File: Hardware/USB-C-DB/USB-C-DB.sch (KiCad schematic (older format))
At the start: 2 parts

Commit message: Updating schematic to v0.2 > Added USB to UART bridge and initial biasing > Added biasing circuitry for MCU > Moved display section to hierarchy > Simplified and consolidated power supply section > Added bypass caps for power supplies, USB interface IC and MCU
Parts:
- removed U?: PIC18F25K50-xSO, Package_SO:SOIC-28W_7.5x17.9mm_P1.27mm, symbol MCU_Microchip_PIC18:PIC18F25K50-xSO
- added C? (x6): 0.1u, Capacitor_SMD:C_0805_2012Metric_Pad1.18x1.45mm_HandSolder, symbol Device:C
- added C? (x3): 10u, Capacitor_SMD:C_0805_2012Metric_Pad1.18x1.45mm_HandSolder, symbol Device:C
- added C? (x2): 47p, Capacitor_SMD:C_0402_1005Metric_Pad0.74x0.62mm_HandSolder, symbol Device:C
- added C? (x4): 4.7u, Capacitor_SMD:C_0805_2012Metric_Pad1.18x1.45mm_HandSolder, symbol Device:C
- added J2: BatTP+, TestPoint:TestPoint_Pad_4.0x4.0mm, symbol Connector_Generic:Conn_01x01
- added J3: JST Battery con, Connector_JST:JST_PH_B2B-PH-K_1x02_P2.00mm_Vertical, symbol Connector_Generic:Conn_01x02
- added J4: BatTP-, TestPoint:TestPoint_Pad_4.0x4.0mm, symbol Connector_Generic:Conn_01x01
- added R? (x3): 5.1k, Resistor_SMD:R_0805_2012Metric_Pad1.20x1.40mm_HandSolder, symbol Device:R
- added R? (x7): 10k, Resistor_SMD:R_0603_1608Metric_Pad0.98x0.95mm_HandSolder, symbol Device:R
- added R?: 0.001, Resistor_SMD:R_2512_6332Metric_Pad1.40x3.35mm_HandSolder, symbol Device:R_Shunt
- added U1: FT260S-U, Package_SO:TSSOP-28_4.4x9.7mm_P0.65mm, symbol FT260S-U:FT260S-U
- added U3: ESP-WROOM-02, RF_Module:ESP-WROOM-02, symbol RF_Module:ESP-WROOM-02
- added U?: LD1117S33TR_SOT223, Package_TO_SOT_SMD:SOT-223-3_TabPin2, symbol Regulator_Linear:LD1117S33TR_SOT223
- J1: renamed from J?; symbol Connector:USB_C_Receptacle -> USB-C-DB-rescue:USB_C_Receptacle-Connector
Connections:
- net labels added: +3.3V, +BATT, -BATT, GND, MCU_EN, MCU_IO12, MCU_IO13, MCU_IO14, MCU_IO16, MCU_IO4, MCU_IO5, MCU_RESET, RESETN, STEST_RSTN, UART_RX_N, UART_TX_P, USB2_N, USB2_P, VBUS, VBUS_SENSEN, VBUS_SENSEP, VCCIO, VOUT3V3
- wire segments 0 -> 152
- no-connect marks 0 -> 10
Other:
- note added: "18-12-2021"
- note added: "3.3V supply rail generation for ESP module"
- note added: "Add 33 ohm series resistors?"
- note added: "Battery connector"
- note added: "Bypass caps for MCU"
- note added: "Bypass caps for USB interface IC"
- note added: "Current sence resistor to detect\n USB power draw above 2.5W\n and throttle power to comply\n with the USB 2.0 spec."
- note added: "Display and controller hierarchy"
- note added: "ESP micro-controller"
- note added: "Negotiate up current but stick to 5V bus"
- note added: "Pull DCNF1 HIGH and DCNF0 LOW\n to enable only UART\n (DIO3 as RXD, DIO4 as TXD)"
- note added: "Total power with 80 RGB LEDs comes out to be\n around 1W (821mW Typ, 1.5W Max). Use fixed\n termination for requesting USB power state\n rather than using controller."
- note added: "v0.2"
- note removed: "03-09-2021"
- note removed: "v1.0"

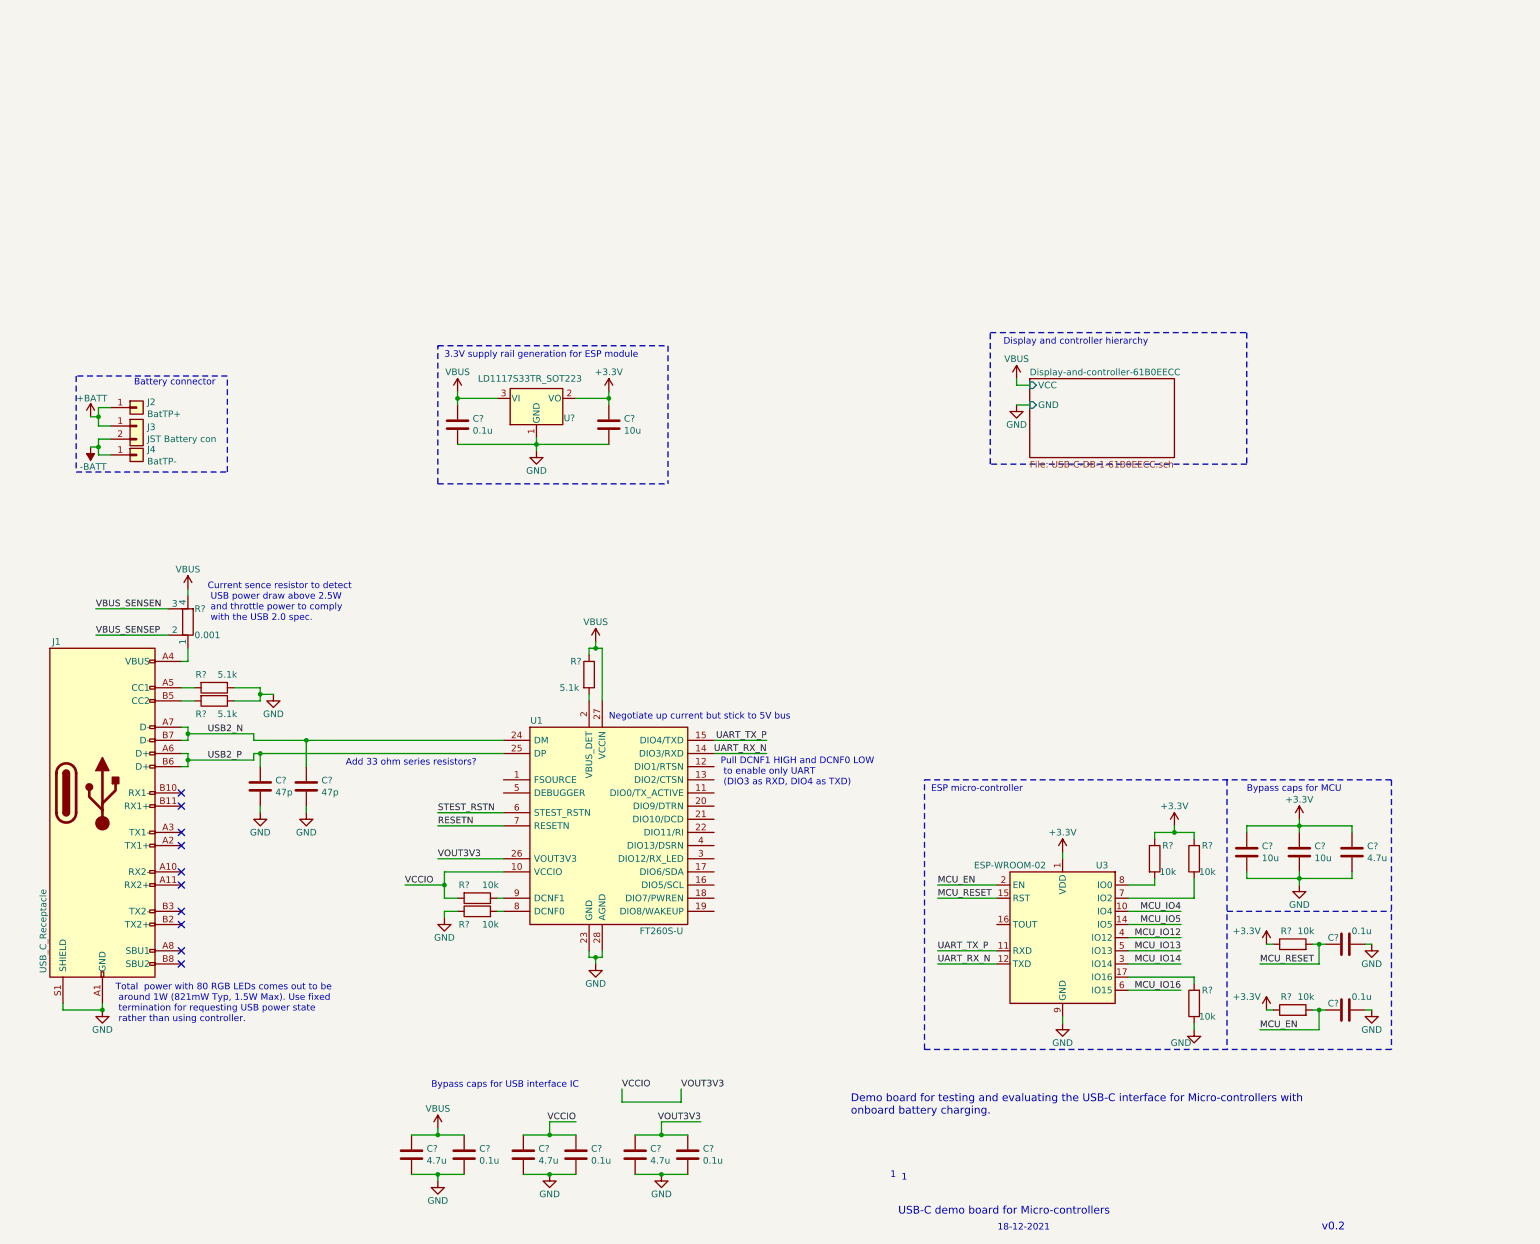
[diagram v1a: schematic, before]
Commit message: Wiring up USB interface (schematic v0.3) > Adding ESD circuity for USB interface > Adding remaining bias and configuration circuity for the UBS interface IC
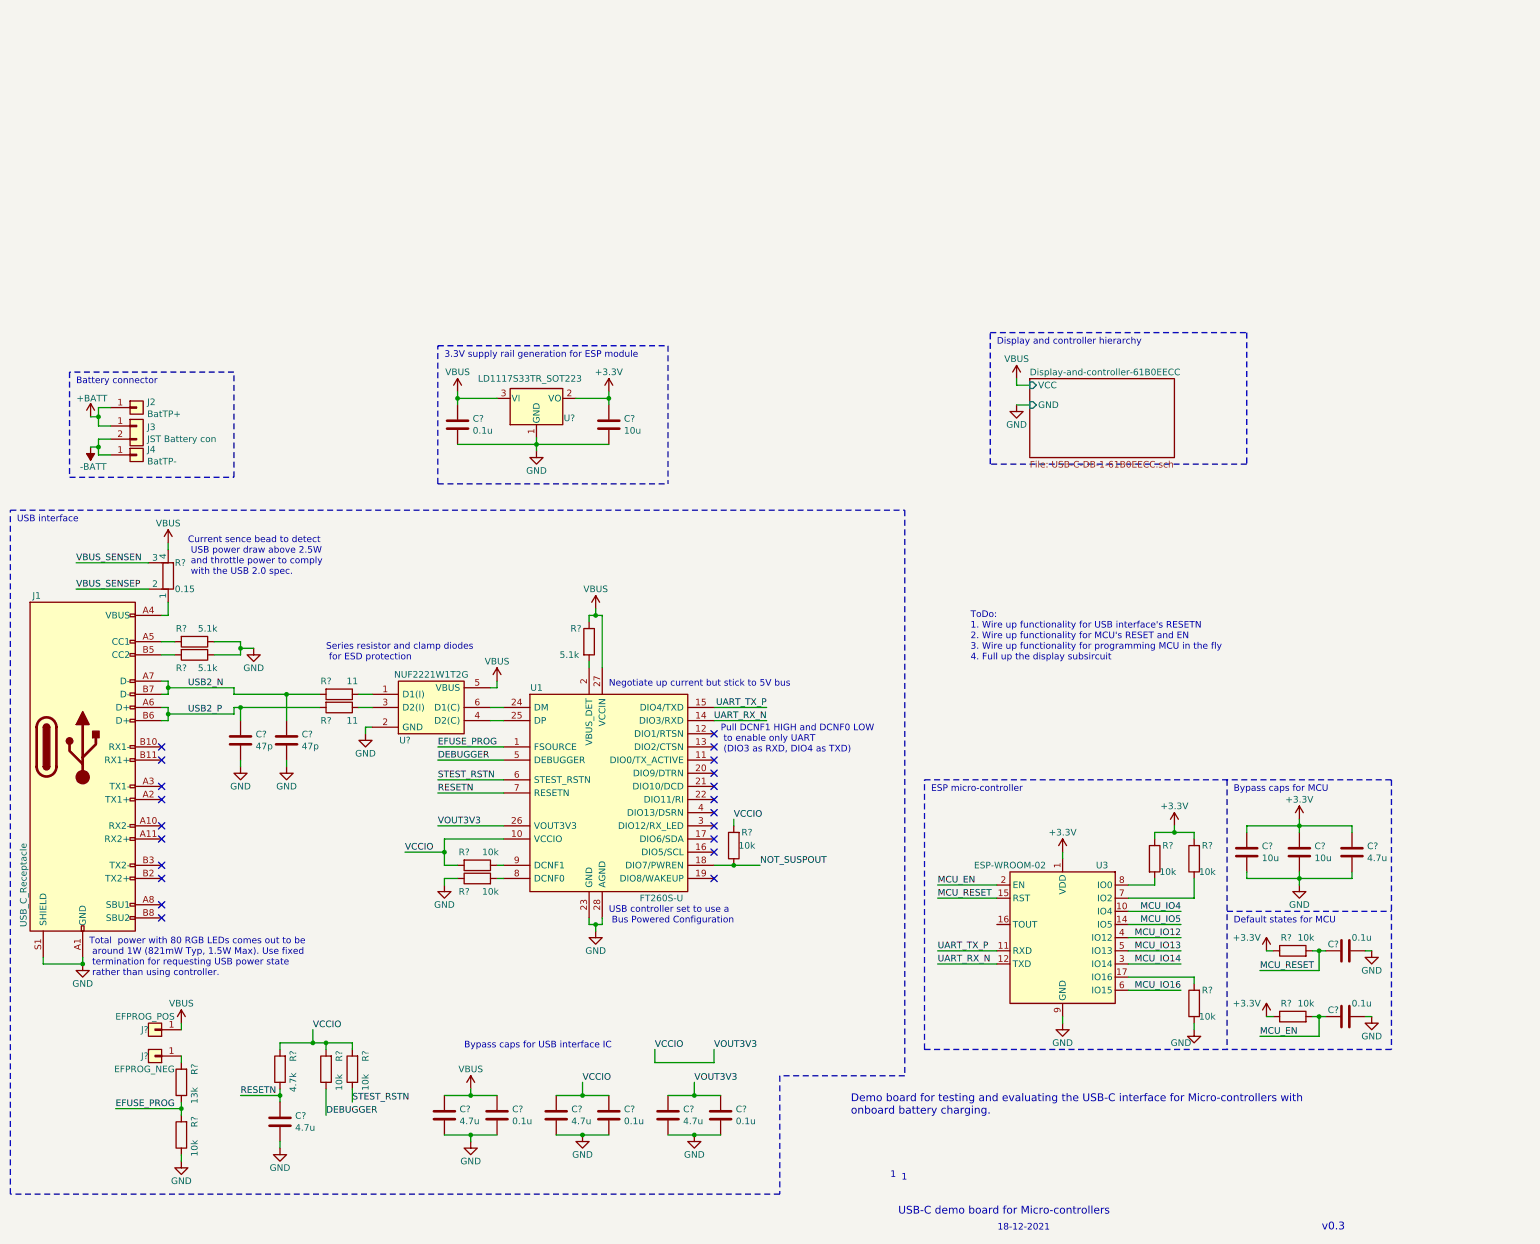
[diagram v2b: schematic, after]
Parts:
- removed U1: FT260S-U, Package_SO:TSSOP-28_4.4x9.7mm_P0.65mm, symbol FT260S-U:FT260S-U
- added C?: 4.7u, Capacitor_SMD:C_0805_2012Metric_Pad1.18x1.45mm_HandSolder, symbol Device:C
- added J?: EFPROG_POS, TestPoint:TestPoint_Pad_4.0x4.0mm, symbol Connector_Generic:Conn_01x01
- added J?: EFPROG_NEG, TestPoint:TestPoint_Pad_4.0x4.0mm, symbol Connector_Generic:Conn_01x01
- added R? (x4): 10k, Resistor_SMD:R_0603_1608Metric_Pad0.98x0.95mm_HandSolder, symbol Device:R
- added R?: 4.7k, Resistor_SMD:R_0805_2012Metric_Pad1.20x1.40mm_HandSolder, symbol Device:R
- added R?: 13k, Resistor_SMD:R_0805_2012Metric_Pad1.20x1.40mm_HandSolder, symbol Device:R
- added R? (x2): 11, Resistor_SMD:R_0402_1005Metric_Pad0.72x0.64mm_HandSolder, symbol Device:R
- added U1: FT260S-U, Mouser-imports:SOP65P640X120-28N, symbol USB-C-DB-rescue:FT260S-U
- added U?: NUF2221W1T2G, SOT65P210X110-6N, symbol USB-C-DB-rescue:NUF2221W1T2G
- R?: value 0.001 -> 0.15; footprint Resistor_SMD:R_2512_6332Metric_Pad1.40x3.35mm_HandSolder -> Resistor_SMD:R_0603_1608Metric_Pad0.98x0.95mm_HandSolder; MPN PA2512FKE070R001E -> KPZ1608SHR601ATD25
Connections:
- net GND: now also C?.2, R?.1, U1.23 (GND), U1.28 (AGND), U?.2 (GND)
- net RESETN: now also C?.1, R?.1, U1.7 (RESETN)
- net STEST_RSTN: now also R?.1, U1.6 (STEST_RSTN)
- net UART_RX_N: now also U1.14 (DIO3/RXD)
- net UART_TX_P: now also U1.15 (DIO4/TXD)
- net USB2_N: now also R?.2
- net USB2_P: now also R?.2
- net VBUS: now also J?.1 (Pin_1), U1.27 (VCCIN), U?.5 (VBUS)
- net VCCIO: now also R?.2, R?.2, R?.2, R?.2, U1.10 (VCCIO), U1.26 (VOUT3V3)
- net at R?.2: now also U1.2 (VBUS_DET)
- net at R?.2: now also U1.8 (DCNF0)
- net at R?.1: now also U1.9 (DCNF1)
- new net: J?.1 (Pin_1), R?.2
- new net: R?.1, U?.1 (D1(I))
- new net: U1.24 (DM), U?.6 (D1(C))
- new net: U1.25 (DP), U?.4 (D2(C))
- new net: R?.1, U?.3 (D2(I))
- new net DEBUGGER: R?.1, U1.5 (DEBUGGER)
- new net EFUSE_PROG: R?.1, R?.2, U1.1 (FSOURCE)
- new net NOT_SUSPOUT: R?.1, U1.18 (DIO7/PWREN)
- no-connect marks 10 -> 21
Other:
- note added: "Current sence bead to detect\n USB power draw above 2.5W\n and throttle power to comply\n with the USB 2.0 spec."
- note added: "Default states for MCU"
- note added: "Series resistor and clamp diodes\n for ESD protection"
- note added: "ToDo:\n1. Wire up functionality for USB interface's RESETN\n2. Wire up functionality for MCU's RESET and EN\n3. Wire up functionality for programming MCU in the fly\n4. Full up the display subsircuit"
- note added: "USB controller set to use a\n Bus Powered Configuration"
- note added: "USB interface"
- note added: "v0.3"
- note removed: "Add 33 ohm series resistors?"
- note removed: "Current sence resistor to detect\n USB power draw above 2.5W\n and throttle power to comply\n with the USB 2.0 spec."
- note removed: "v0.2"
- moved on the sheet: C?, J1, R?
